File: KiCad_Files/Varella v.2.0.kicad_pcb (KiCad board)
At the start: 4 copper layers, 86 x 86 mm, 97 parts, among them IC1 MAX6682MUA+T, IC2 MAX6682MUA+T, IC3 MAX6682MUA+T, IC4 MMC5983MA, IC5 ZMOD4410AI3V, J1 ESQ-120-39-G-D, J2 Conn_01x12_Male, J3 MEM2075-00-140-01-A, J4 53261-7002, J5 53261-7002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

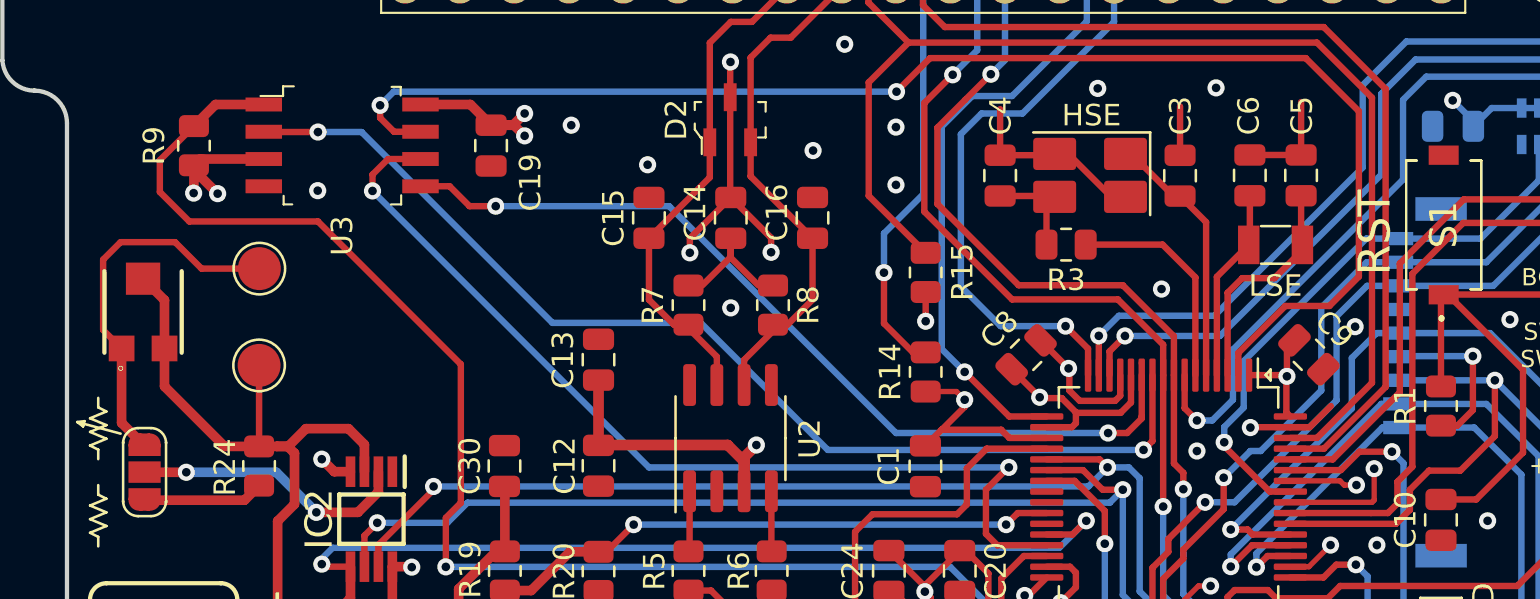
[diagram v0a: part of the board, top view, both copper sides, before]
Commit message: Update RTC Battery Silk Screen name
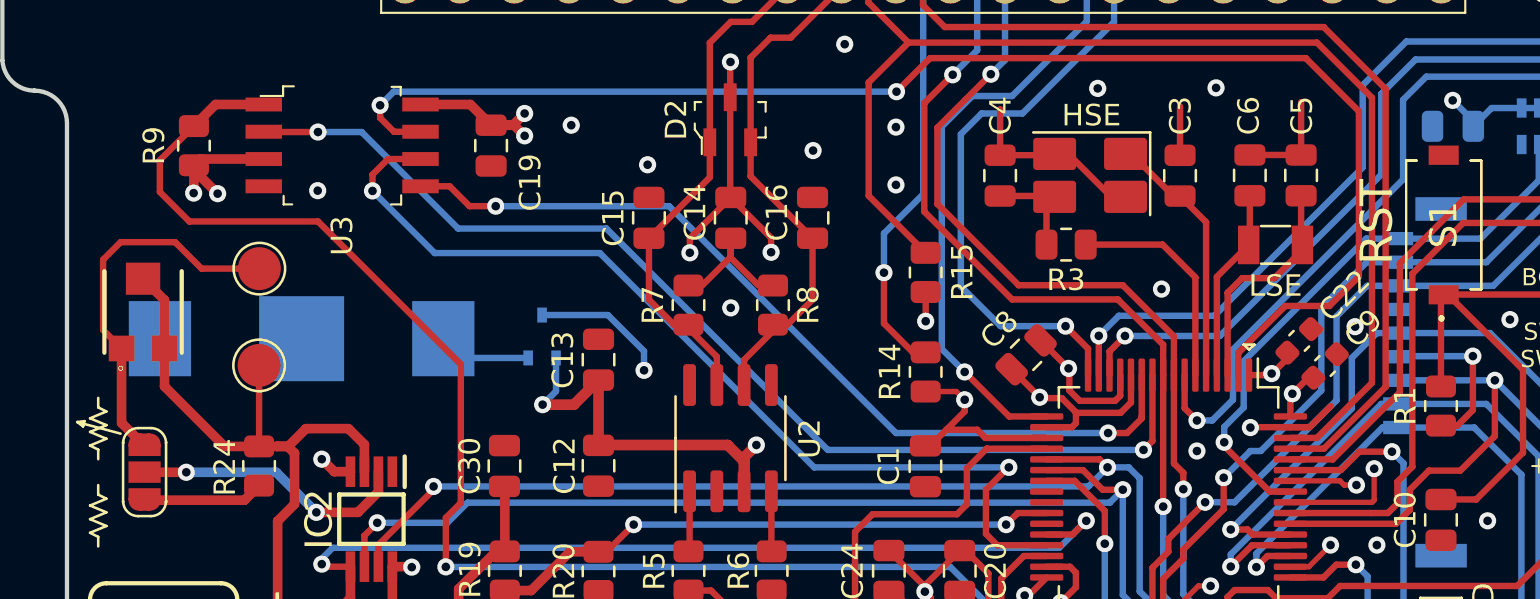
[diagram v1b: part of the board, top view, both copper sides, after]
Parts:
- added BT1: Battery_Cell, SamacSys_Parts:3030, B.Cu at (130.0, 79.7)
- added C22: 100n, Capacitor_SMD:C_0603_1608Metric, F.Cu at (176.5, 79.8)
- added D3: BAT54CW, Package_TO_SOT_SMD:SOT-323_SC-70, B.Cu at (141.2, 79.6)
- C9: footprint Capacitor_SMD:C_0805_2012Metric -> Capacitor_SMD:C_0603_1608Metric
- moved C9 0.92 mm to (177.7, 81.0), turned to 45 degrees
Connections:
- U1 pad 1: 3V3 -> RTC_BAT
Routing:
- net RTC_BAT: track 0.00 -> 40.6 mm, vias 0 -> 2
- net Net-(BT1-Pad1): track 0.00 -> 4.32 mm
- net 3V3: track 179.6 -> 181.8 mm, vias 36 -> 37
- net GND: vias 58 -> 56
- net (no net): vias 0 -> 2
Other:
- board text added: "RTC-BAT"

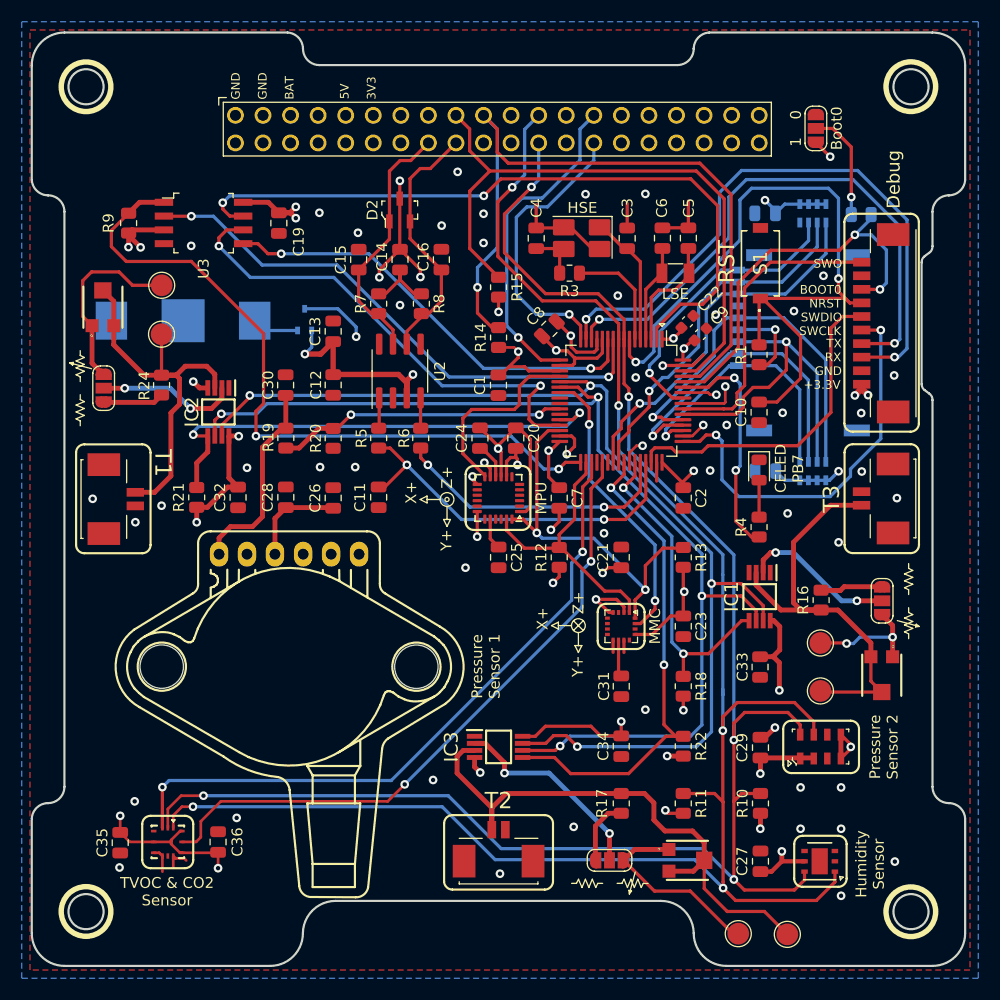
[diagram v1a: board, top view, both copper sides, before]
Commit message: Add 1,024 V voltage reference for the ADC.
We realised that the MPX5700 barometer would only output a voltage from 0 to 0,66 V in the altitude range of the radiosonde trajectory. By adding this voltage reference to the ADC we will have much better precision on pressure readings.
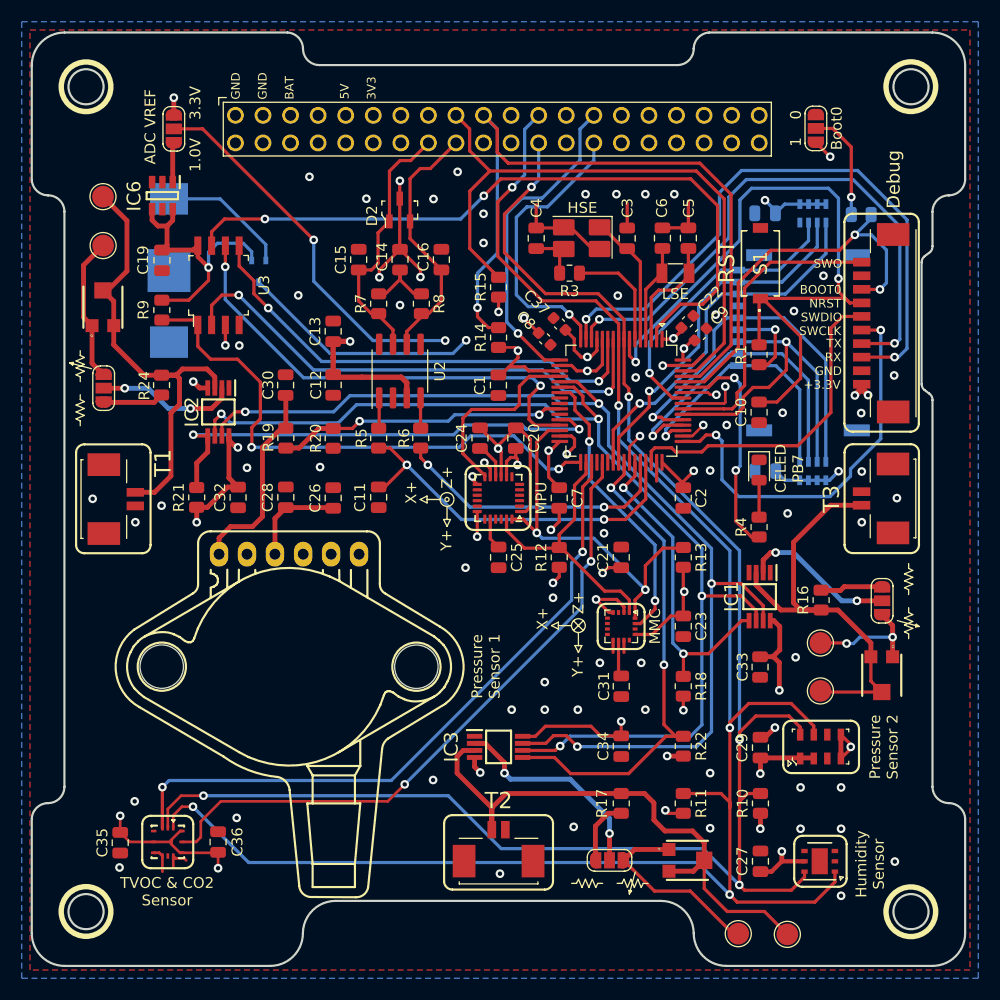
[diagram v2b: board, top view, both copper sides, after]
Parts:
- added C37: 1n, Capacitor_SMD:C_0603_1608Metric, F.Cu at (164.7, 80.0)
- added IC6: MCP1501T-10E_CHY, SamacSys_Parts:SOT95P280X145-6N, F.Cu at (128.1, 68.2)
- added JP5: SolderJumper_3_Open, Jumper:SolderJumper-3_P1.3mm_Open_RoundedPad1.0x1.5mm_NumberLabels, F.Cu at (129.1, 62.1)
- C8: footprint Capacitor_SMD:C_0805_2012Metric -> Capacitor_SMD:C_0603_1608Metric
- moved TP2 13.8 mm to (122.6, 68.3)
- moved C19 11.3 mm to (128.1, 74.2)
- moved R9 8.58 mm to (128.0, 78.8), turned to 90 degrees
- moved TP1 6.52 mm to (122.6, 72.8)
- moved D3 6.14 mm to (137.0, 75.2), turned to 270 degrees
- moved U3 5.90 mm to (133.3, 76.5), turned to 0 degrees
- moved BT1 4.80 mm to (128.7, 75.1), turned to 270 degrees
- moved C8 1.02 mm to (163.3, 81.4), turned to 315 degrees
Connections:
- U1 pad 13: 3V3 -> VREF_1V
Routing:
- net VREF_1V: track 0.00 -> 56.2 mm, vias 0 -> 3
- net FLASH_NSS: track 65.9 -> 51.2 mm
- net Net-(BT1-Pad1): track 4.32 -> 13.1 mm
- net Net-(IC2-Pad3): track 35.6 -> 42.4 mm
- net 3V3: track 181.8 -> 187.0 mm, vias 37 -> 35
- net RTC_BAT: track 40.6 -> 45.7 mm
- net Net-(JP3-Pad3): track 17.6 -> 13.3 mm
- net FLASH_SPI_MOSI: track 40.7 -> 44.4 mm
- net Net-(IC6-Pad1): track 0.00 -> 3.65 mm
- net FLASH_SPI_MISO: track 50.8 -> 47.5 mm
- net GND: track 82.8 -> 79.7 mm, vias 56 -> 70
- net EPS_ALRT1: track 40.2 -> 41.6 mm
- net SCL_A: track 158.6 -> 157.3 mm
- net FLASH_SPI_CLK: track 44.9 -> 43.9 mm
- net Net-(IC3-Pad2): track 18.9 -> 19.7 mm
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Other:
- board text added: "1.0V"
- board text added: "3.3V"
- board text added: "ADC VREF"

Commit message: Reroutes voltage reference selector trace for better aesthetics.
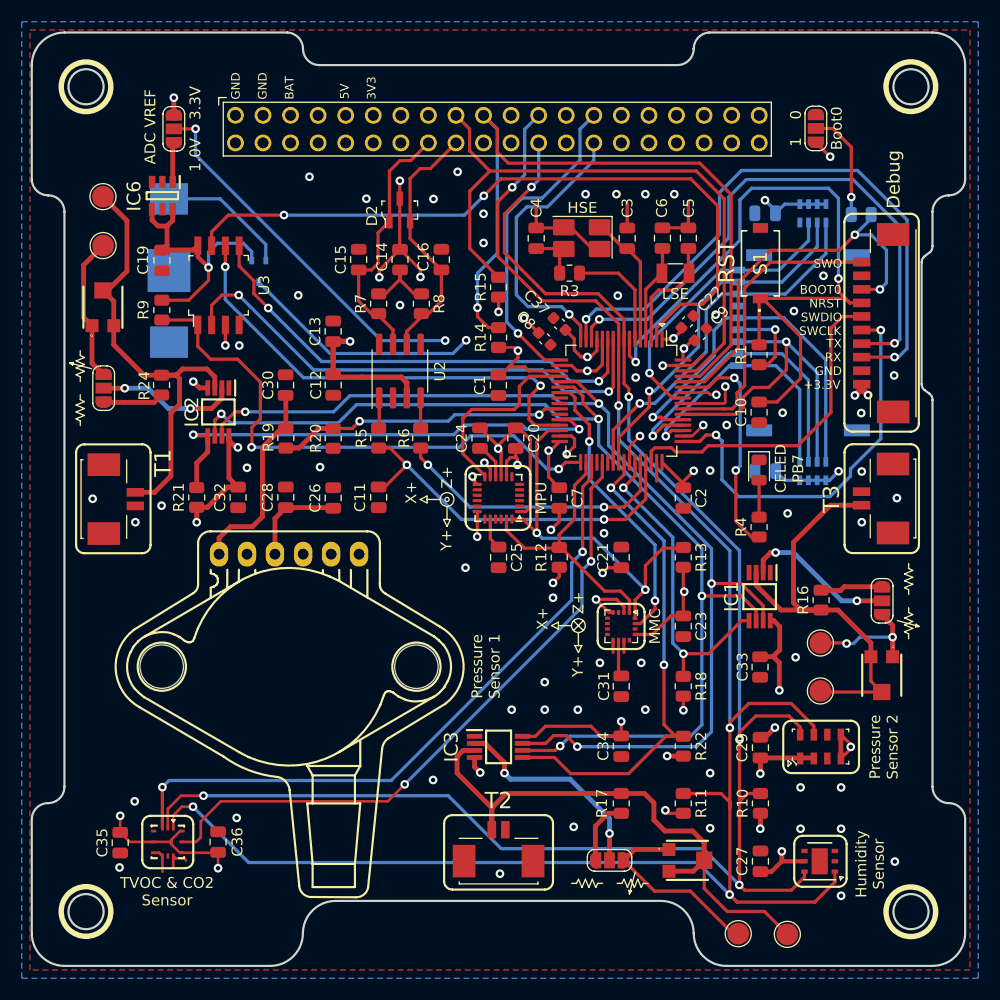
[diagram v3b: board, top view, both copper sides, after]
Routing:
- net VREF_1V: track 56.2 -> 55.4 mm

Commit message: Change silkscreen
Adds the name "Varela" to the board.
Also adds the name of the designer (me).
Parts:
- added G***: LOGO, Caurin_Footprints:Logo_10,8mm, F.Cu at (122.3, 119.0)
- added G***: LOGO, LogosZenith:VarelaLogov2_noyear_2,7mm, B.Cu at (159.5, 72.5)
- added REF**: ESD-Logo_6.6x6mm_SilkScreen, Symbol:ESD-Logo_6.6x6mm_SilkScreen, F.Cu at (139.3, 70.2)
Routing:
- net FLASH_NRST: track 66.8 -> 67.8 mm
- net VREF_1V: track 55.4 -> 56.0 mm
- net 5V: track 52.8 -> 52.2 mm
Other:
- board text added: "CAN"
- board text added: "Flash"
- board text added: "Projetista: Júlio Calandrin :)"
- board text added: "github.com/zenitheesc/Probe-RAS"
